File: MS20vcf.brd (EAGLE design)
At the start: 39.4 x 98.7 mm, 45 parts, among them IC1 LM13700N, IC2 TL074P, Q1 BC558B, Q2 BC558B

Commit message: Moved C3 to clear potentiometer, added value labels to potentiometers.
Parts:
- moved C3 1.42 mm to (21.6, 36.8)
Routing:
- net N$8: track 24.6 -> 26.1 mm
- net +12V: track 65.1 -> 66.5 mm
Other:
- board text added: "A100k"
- board text added: "B10k"
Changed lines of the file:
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@@
 <?xml version="1.0" encoding="utf-8"?>
 <!DOCTYPE eagle SYSTEM "eagle.dtd">
-<eagle version="8.3.0">
+<eagle version="8.3.1">
 <drawing>
 <settings>
@@
 VCF</text>
 <text x="38.1" y="92.075" size="0.8128" layer="25" font="vector" ratio="10" rot="R270">v1.0 20170810</text>
+<text x="5.08" y="28.575" size="1.6764" layer="21" font="vector" ratio="10">B10k</text>
+<text x="17.78" y="28.575" size="1.6764" layer="21" font="vector" ratio="10">B10k</text>
+<text x="17.78" y="79.375" size="1.6764" layer="21" font="vector" ratio="10">B10k</text>
+<text x="24.13" y="48.895" size="1.6764" layer="21" font="vector" ratio="10">A100k</text>
 </plain>
 <attributes>
@@
 <attribute name="VALUE" x="32.131" y="50.546" size="0.8128" layer="27" ratio="10"/>
 </element>
-<element name="C3" library="rcl" library_urn="urn:adsk.eagle:library:334" package="C050-025X075" value="1n" x="22.225" y="38.1" smashed="yes" rot="R270">
-<attribute name="NAME" x="21.336" y="33.401" size="0.8128" layer="25" ratio="10"/>
-<attribute name="VALUE" x="19.431" y="41.529" size="0.8128" layer="27" ratio="10" rot="R270"/>
+<element name="C3" library="rcl" library_urn="urn:adsk.eagle:library:334" package="C050-025X075" value="1n" x="21.59" y="36.83" smashed="yes" rot="R270">
+<attribute name="NAME" x="20.701" y="32.131" size="0.8128" layer="25" ratio="10"/>
+<attribute name="VALUE" x="18.796" y="40.259" size="0.8128" layer="27" ratio="10" rot="R270"/>
 </element>
 <element name="C4" library="rcl" library_urn="urn:adsk.eagle:library:334" package="C050-025X075" value="470n" x="29.21" y="35.56" smashed="yes" rot="R180">
@@
 <contactref element="IC2" pad="3"/>
 <contactref element="C3" pad="1"/>
-<wire x1="20.955" y1="41.91" x2="22.225" y2="40.64" width="0.254" layer="1"/>
-<wire x1="20.955" y1="41.91" x2="19.05" y2="41.91" width="0.254" layer="1"/>
 <wire x1="27.94" y1="58.42" x2="27.94" y2="55.245" width="0.254" layer="1"/>
 <wire x1="26.67" y1="53.975" x2="27.94" y2="55.245" width="0.254" layer="1"/>
-<wire x1="22.225" y1="40.64" x2="23.495" y2="41.91" width="0.254" layer="1"/>
-<wire x1="23.495" y1="41.91" x2="24.765" y2="41.91" width="0.254" layer="1"/>
 <wire x1="24.765" y1="41.91" x2="26.67" y2="43.815" width="0.254" layer="1"/>
 <wire x1="26.67" y1="43.815" x2="26.67" y2="53.975" width="0.254" layer="1"/>
+<wire x1="21.647540625" y1="41.91" x2="19.05" y2="41.91" width="0.254" layer="1"/>
+<wire x1="21.647540625" y1="41.91" x2="24.765" y2="41.91" width="0.254" layer="1"/>
+<wire x1="21.59" y1="39.37" x2="21.59" y2="41.852459375" width="0.254" layer="1"/>
+<wire x1="21.59" y1="41.852459375" x2="21.647540625" y2="41.91" width="0.254" layer="1"/>
 </signal>
 <signal name="N$9">
@@
 <wire x1="30.48" y1="58.42" x2="30.48" y2="56.515" width="0.254" layer="1"/>
 <wire x1="27.305" y1="53.34" x2="30.48" y2="56.515" width="0.254" layer="1"/>
-<wire x1="19.05" y1="39.37" x2="22.86" y2="39.37" width="0.254" layer="1"/>
 <wire x1="25.4" y1="83.82" x2="22.86" y2="83.82" width="0.508" layer="1"/>
 <wire x1="25.4" y1="83.82" x2="25.4" y2="82.55" width="0.4064" layer="16"/>
@@
 <wire x1="22.82" y1="69.255" x2="24.13" y2="67.945" width="0.4064" layer="1"/>
 <wire x1="30.48" y1="59.055" x2="30.48" y2="58.42" width="0.4064" layer="1"/>
-<wire x1="22.86" y1="39.37" x2="24.13" y2="40.64" width="0.254" layer="1"/>
 <wire x1="24.13" y1="40.64" x2="24.765" y2="40.64" width="0.254" layer="1"/>
 <wire x1="24.765" y1="40.64" x2="27.305" y2="43.18" width="0.254" layer="1"/>
@@
 <wire x1="27.94" y1="87.63" x2="25.4" y2="85.09" width="0.508" layer="1"/>
 <wire x1="25.4" y1="85.09" x2="25.4" y2="83.82" width="0.508" layer="1"/>
+<wire x1="19.05" y1="39.37" x2="19.685" y2="39.37" width="0.254" layer="1"/>
+<wire x1="19.685" y1="39.37" x2="20.955" y2="38.1" width="0.254" layer="1"/>
+<wire x1="20.955" y1="38.1" x2="22.225" y2="38.1" width="0.254" layer="1"/>
+<wire x1="22.225" y1="38.1" x2="22.86" y2="38.735" width="0.254" layer="1"/>
+<wire x1="22.86" y1="38.735" x2="22.86" y2="39.37" width="0.254" layer="1"/>
+<wire x1="22.86" y1="39.37" x2="24.13" y2="40.64" width="0.254" layer="1"/>
 </signal>
 <signal name="N$23">

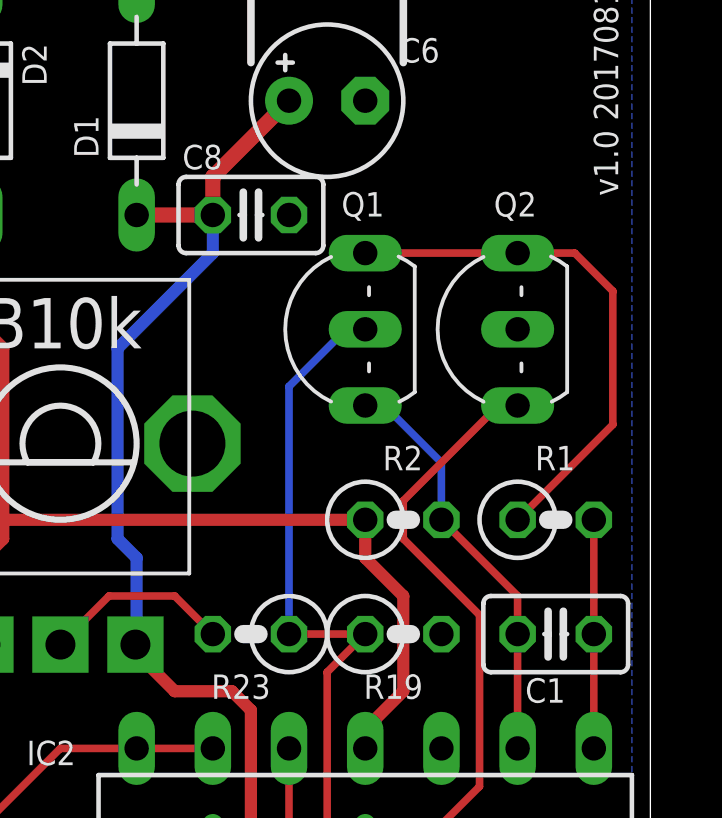
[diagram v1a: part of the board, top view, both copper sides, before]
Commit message: Moved transistor pair closer.
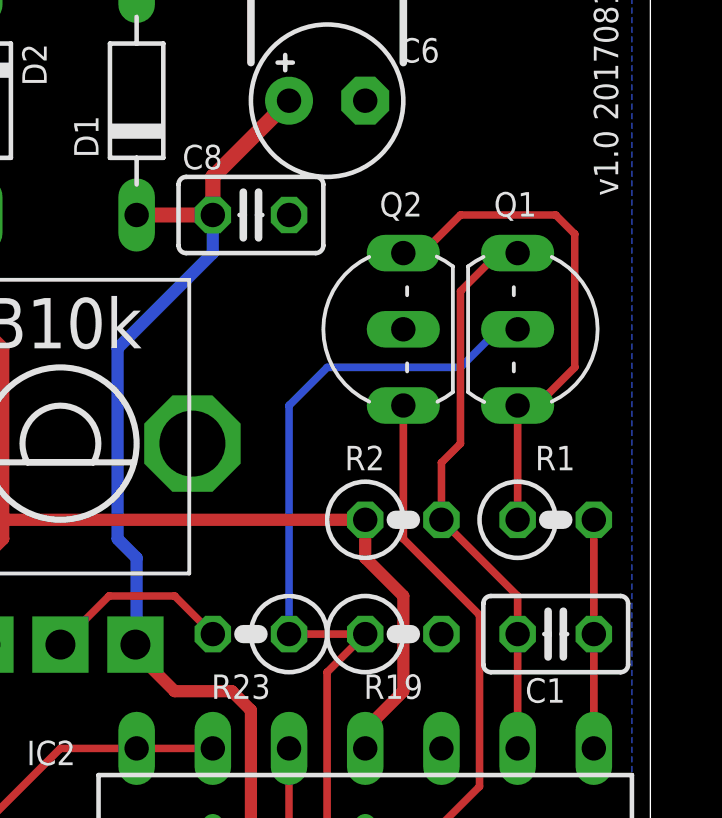
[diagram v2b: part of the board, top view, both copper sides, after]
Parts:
- moved Q1 7.62 mm to (36.8, 80.0), turned to 270 degrees
- moved Q2 3.81 mm to (30.5, 80.0)
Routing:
- net N$3: track 13.9 -> 19.0 mm
- net N$20: track 98.9 -> 103.6 mm
- net N$4: track 37.4 -> 35.4 mm
- net N$2: track 17.7 -> 17.2 mm
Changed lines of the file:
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@@
 <?xml version="1.0" encoding="utf-8"?>
 <!DOCTYPE eagle SYSTEM "eagle.dtd">
-<eagle version="8.3.1">
+<eagle version="9.4.0">
 <drawing>
 <settings>
@@
 <param name="dpMaxLengthDifference" value="10mm"/>
 <param name="dpGapFactor" value="2.5"/>
-<param name="checkGrid" value="0"/>
 <param name="checkAngle" value="0"/>
 <param name="checkFont" value="1"/>
 <param name="checkRestrict" value="1"/>
+<param name="checkStop" value="0"/>
+<param name="checkValues" value="0"/>
+<param name="checkNames" value="1"/>
+<param name="checkWireStubs" value="1"/>
+<param name="checkPolygonWidth" value="0"/>
 <param name="useDiameter" value="13"/>
 <param name="maxErrors" value="50"/>
@@
 <attribute name="VALUE" x="38.735" y="44.069" size="0.8128" layer="27" ratio="10"/>
 </element>
-<element name="Q1" library="transistor-pnp" library_urn="urn:adsk.eagle:library:399" package="TO92-EBC" value="BC558B" x="29.21" y="80.01" smashed="yes" rot="R90">
-<attribute name="NAME" x="31.115" y="84.582" size="0.8128" layer="25" ratio="10" rot="R180"/>
-<attribute name="VALUE" x="33.782" y="77.47" size="0.8128" layer="27" ratio="10" rot="R90"/>
-</element>
-<element name="Q2" library="transistor-pnp" library_urn="urn:adsk.eagle:library:399" package="TO92-EBC" value="BC558B" x="34.29" y="80.01" smashed="yes" rot="R90">
+<element name="Q1" library="transistor-pnp" library_urn="urn:adsk.eagle:library:399" package="TO92-EBC" value="BC558B" x="36.83" y="80.01" smashed="yes" rot="R270">
 <attribute name="NAME" x="36.195" y="84.582" size="0.8128" layer="25" ratio="10" rot="R180"/>
-<attribute name="VALUE" x="38.862" y="77.47" size="0.8128" layer="27" ratio="10" rot="R90"/>
+<attribute name="VALUE" x="32.258" y="82.55" size="0.8128" layer="27" ratio="10" rot="R270"/>
+</element>
+<element name="Q2" library="transistor-pnp" library_urn="urn:adsk.eagle:library:399" package="TO92-EBC" value="BC558B" x="30.48" y="80.01" smashed="yes" rot="R90">
+<attribute name="NAME" x="32.385" y="84.582" size="0.8128" layer="25" ratio="10" rot="R180"/>
+<attribute name="VALUE" x="35.052" y="77.47" size="0.8128" layer="27" ratio="10" rot="R90"/>
 </element>
 <element name="R1" library="rcl" library_urn="urn:adsk.eagle:library:334" package="0207/2V" value="4k7" x="36.83" y="73.66" smashed="yes">
@@
 </element>
 <element name="R2" library="rcl" library_urn="urn:adsk.eagle:library:334" package="0207/2V" value="470k" x="31.75" y="73.66" smashed="yes">
-<attribute name="NAME" x="31.0642" y="75.311" size="0.8128" layer="25" ratio="10"/>
+<attribute name="NAME" x="29.7942" y="75.311" size="0.8128" layer="25" ratio="10"/>
 <attribute name="VALUE" x="31.6992" y="71.4248" size="0.8128" layer="27" ratio="10"/>
 </element>
@@
 <contactref element="Q2" pad="E"/>
 <contactref element="R1" pad="1"/>
-<wire x1="30.48" y1="82.55" x2="35.56" y2="82.55" width="0.254" layer="1"/>
-<wire x1="35.56" y1="82.55" x2="37.465" y2="82.55" width="0.254" layer="1"/>
-<wire x1="37.465" y1="82.55" x2="38.735" y2="81.28" width="0.254" layer="1"/>
-<wire x1="38.735" y1="81.28" x2="38.735" y2="76.835" width="0.254" layer="1"/>
-<wire x1="38.735" y1="76.835" x2="35.56" y2="73.66" width="0.254" layer="1"/>
+<wire x1="35.56" y1="73.66" x2="35.56" y2="77.47" width="0.254" layer="1"/>
+<wire x1="35.56" y1="77.47" x2="36.195" y2="77.47" width="0.254" layer="1"/>
+<wire x1="36.195" y1="77.47" x2="37.465" y2="78.74" width="0.254" layer="1"/>
+<wire x1="37.465" y1="78.74" x2="37.465" y2="83.185" width="0.254" layer="1"/>
+<wire x1="37.465" y1="83.185" x2="36.83" y2="83.82" width="0.254" layer="1"/>
+<wire x1="36.83" y1="83.82" x2="33.655" y2="83.82" width="0.254" layer="1"/>
+<wire x1="33.655" y1="83.82" x2="32.385" y2="82.55" width="0.254" layer="1"/>
+<wire x1="32.385" y1="82.55" x2="31.75" y2="82.55" width="0.254" layer="1"/>
 </signal>
 <signal name="N$3">
@@
 <wire x1="33.02" y1="73.66" x2="35.56" y2="71.12" width="0.254" layer="1"/>
 <wire x1="35.56" y1="71.12" x2="35.56" y2="69.85" width="0.254" layer="1"/>
-<wire x1="30.48" y1="77.47" x2="31.115" y2="77.47" width="0.254" layer="16"/>
-<wire x1="31.115" y1="77.47" x2="33.02" y2="75.565" width="0.254" layer="16"/>
-<wire x1="33.02" y1="75.565" x2="33.02" y2="73.66" width="0.254" layer="16"/>
+<wire x1="33.02" y1="73.66" x2="33.02" y2="75.565" width="0.254" layer="1"/>
+<wire x1="33.02" y1="75.565" x2="33.655" y2="76.2" width="0.254" layer="1"/>
+<wire x1="33.655" y1="76.2" x2="33.655" y2="81.28" width="0.254" layer="1"/>
+<wire x1="33.655" y1="81.28" x2="34.925" y2="82.55" width="0.254" layer="1"/>
+<wire x1="34.925" y1="82.55" x2="35.56" y2="82.55" width="0.254" layer="1"/>
 </signal>
 <signal name="-12V">
@@
 <contactref element="R6" pad="2"/>
 <wire x1="17.78" y1="58.42" x2="15.24" y2="58.42" width="0.254" layer="1"/>
-<wire x1="35.56" y1="77.47" x2="34.925" y2="77.47" width="0.254" layer="1"/>
-<wire x1="34.925" y1="77.47" x2="31.75" y2="74.295" width="0.254" layer="1"/>
-<wire x1="31.75" y1="74.295" x2="31.75" y2="73.025" width="0.254" layer="1"/>
-<wire x1="31.75" y1="73.025" x2="34.29" y2="70.485" width="0.254" layer="1"/>
+<wire x1="34.29" y1="70.485" x2="31.75" y2="73.025" width="0.254" layer="1"/>
 <wire x1="34.29" y1="70.485" x2="34.29" y2="64.77" width="0.254" layer="1"/>
 <wire x1="34.29" y1="64.77" x2="33.02" y2="63.5" width="0.254" layer="1"/>
@@
 <wire x1="25.4" y1="63.5" x2="22.86" y2="63.5" width="0.254" layer="1"/>
 <wire x1="22.86" y1="63.5" x2="17.78" y2="58.42" width="0.254" layer="1"/>
+<wire x1="31.75" y1="73.025" x2="31.75" y2="77.47" width="0.254" layer="1"/>
 </signal>
 <signal name="N$5">
@@
 <contactref element="R23" pad="1"/>
 <wire x1="27.94" y1="69.85" x2="30.48" y2="69.85" width="0.254" layer="1"/>
-<wire x1="30.48" y1="80.01" x2="29.845" y2="80.01" width="0.254" layer="16"/>
-<wire x1="27.94" y1="78.105" x2="27.94" y2="69.85" width="0.254" layer="16"/>
-<wire x1="29.845" y1="80.01" x2="27.94" y2="78.105" width="0.254" layer="16"/>
+<wire x1="27.94" y1="69.85" x2="27.94" y2="77.47" width="0.254" layer="16"/>
 <wire x1="30.48" y1="69.85" x2="29.21" y2="68.58" width="0.254" layer="1"/>
 <wire x1="29.21" y1="68.58" x2="29.21" y2="62.865" width="0.254" layer="1"/>
@@
 <wire x1="27.94" y1="16.51" x2="15.3613875" y2="16.51" width="0.254" layer="1"/>
 <wire x1="15.3613875" y1="16.51" x2="15.24" y2="16.3886125" width="0.254" layer="1"/>
+<wire x1="27.94" y1="77.47" x2="29.21" y2="78.74" width="0.254" layer="16"/>
+<wire x1="29.21" y1="78.74" x2="33.655" y2="78.74" width="0.254" layer="16"/>
+<wire x1="33.655" y1="78.74" x2="34.925" y2="80.01" width="0.254" layer="16"/>
+<wire x1="34.925" y1="80.01" x2="35.56" y2="80.01" width="0.254" layer="16"/>
 </signal>
 <signal name="N$21">
@@
 </signal>
 </signals>
+<mfgpreviewcolors>
+<mfgpreviewcolor name="soldermaskcolor" color="0xC8008000"/>
+<mfgpreviewcolor name="silkscreencolor" color="0xFFFEFEFE"/>
+<mfgpreviewcolor name="backgroundcolor" color="0xFF282828"/>
+<mfgpreviewcolor name="coppercolor" color="0xFFFFBF00"/>
+<mfgpreviewcolor name="substratecolor" color="0xFF786E46"/>
+</mfgpreviewcolors>
 </board>
 </drawing>
